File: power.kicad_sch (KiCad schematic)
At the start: 28 parts, among them J3 Conn_01x02_MountingPin, J4 Conn_01x02_Socket, J5 Conn_01x02_Socket, U3 TPS55287, U4 MPM3620A

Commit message: Power board complete v1.0
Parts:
- added C_in1, C_in3, C_in4: 10u, Capacitor_SMD:C_1206_3216Metric, symbol Device:C
- added J5, J6: 5V, Connector_JST:JST_XH_S2B-XH-A_1x02_P2.50mm_Horizontal, symbol Connector:Conn_01x02_Socket
- added J8, J9: 12V, Connector_JST:JST_XH_S2B-XH-A_1x02_P2.50mm_Horizontal, symbol Connector:Conn_01x02_Socket
- added SW1: Pull Tag, LEOS:D2F-FL-A1, symbol Switch:SW_SPDT
- added SW2: Power Switch, Button_Switch_THT:SW_Slide_SPDT_Angled_CK_OS102011MA1Q, symbol Switch:SW_SPDT
- added TP5: 12V Test, TestPoint:TestPoint_Loop_D2.60mm_Drill0.9mm_Beaded, symbol Connector:TestPoint
- added TP6: GND Test Point, TestPoint:TestPoint_Loop_D2.60mm_Drill0.9mm_Beaded, symbol Connector:TestPoint
- C_COMP1: value 36.5n -> 33n; footprint Capacitor_SMD:C_0805_2012Metric -> Capacitor_SMD:C_0603_1608Metric; Digikey (none) -> 1276-2040-1-ND; MPN (none) -> CL10B333KB8NFNC; Manufacturer (none) -> Samsung Electro-Mechanics
- C_COMP2: value 18.2n -> 15n; footprint Capacitor_SMD:C_0805_2012Metric -> Capacitor_SMD:C_0603_1608Metric; Digikey (none) -> 1276-1277-1-ND; MPN (none) -> CL10B153KB8NNNC; Manufacturer (none) -> Samsung Electro-Mechanics
- C_SYNC1: footprint Capacitor_SMD:C_0805_2012Metric -> Capacitor_SMD:C_0603_1608Metric; Digikey (none) -> 1276-1063-1-ND; MPN (none) -> CL10B473KB8NNNC; Manufacturer (none) -> Samsung Electro-Mechanics
- C_VCC1: Digikey (none) -> 1276-2970-1-ND; MPN (none) -> CL21B475KOFNFNE; Manufacturer (none) -> Samsung Electro-Mechanics
- C_in2: value 47u -> 10u; footprint Capacitor_SMD:C_0805_2012Metric -> Capacitor_SMD:C_1206_3216Metric; Digikey (none) -> 1276-6767-1-ND; MPN (none) -> CL31B106KBHNNNE; Manufacturer (none) -> Samsung Electro-Mechanics
- J3: value Conn_01x02_MountingPin -> Power Input; footprint Connector_AMASS:AMASS_XT60IPW-M_1x03_P7.20mm_Horizontal -> LEOS:AMASS_XT60IPW-M_1x03_P7.20mm_Horizontal; symbol Connector_Generic_MountingPin:Conn_01x02_MountingPin -> Connector:Conn_01x02_Socket
- J4: renamed from J5; value Conn_01x02_Socket -> 5V; Digikey (none) -> 455-S2B-XH-A-ND; MPN (none) -> S2B-XH-A; Manufacturer (none) -> JST
- J7: renamed from J4; value Conn_01x02_Socket -> 12V; Digikey (none) -> 455-S2B-XH-A-ND; MPN (none) -> S2B-XH-A; Manufacturer (none) -> JST
- L1: Digikey (none) -> 587-2960-1-ND; MPN (none) -> NRS8030T100MJGJ; Manufacturer (none) -> Taiyo Yuden
- NT1: footprint (none) -> NetTie:NetTie-2_SMD_Pad0.5mm
- R5, R6, RUP1: Digikey (none) -> 541-100KCCT-ND; MPN (none) -> CRCW0805100KFKEA; Manufacturer (none) -> Vishay Dale
- R7: Digikey (none) -> 541-19.1KCCT-ND; MPN (none) -> CRCW080519K1FKEA; Manufacturer (none) -> Vishay Dale
- RBT1: value 11.1k -> 11k; Digikey (none) -> 541-CRCW080511K0FKEACCT-ND; MPN (none) -> CRCW080511K0FKEAC; Manufacturer (none) -> Vishay Dale
- RP1: value 10k -> 11k; symbol Device:R_US -> Device:R; Digikey (none) -> 541-CRCW080511K0FKEACCT-ND; MPN (none) -> CRCW080511K0FKEAC; Manufacturer (none) -> Vishay Dale
- R_CDC1: Digikey (none) -> 541-20.0KCCT-ND; MPN (none) -> CRCW080520K0FKEA; Manufacturer (none) -> Vishay Dale
- R_COMP1: value 7.23k -> 7.5k; Digikey (none) -> 541-CRCW08057K50FKEACCT-ND; MPN (none) -> CRCW08057K50FKEAC; Manufacturer (none) -> Vishay Dale
- R_FSW1: value 9.3k -> 9.1k; Digikey (none) -> 541-9.10KCCT-ND; MPN (none) -> CRCW08059K10FKEA; Manufacturer (none) -> Vishay Dale
- R_SNS1: Digikey (none) -> 541-WSLP0805R0160FEACT-ND; MPN (none) -> WSLP0805R0160FEA; Manufacturer (none) -> Vishay Dale
- renumbered Cout1 to C_out1
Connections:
- net +12V: now also J8.1 (Pin_1), J9.1 (Pin_1), TP5.1
- net +5V: now also J5.1 (Pin_1), J6.1 (Pin_1)
- net GND: now also C_VCC1.2, C_in1.2, C_in3.2, C_in4.2, J5.2 (Pin_2), J6.2 (Pin_2), J8.2 (Pin_2), J9.2 (Pin_2), SW1.2 (B), SW2.3 (C), TP6.1
- net GNDA: no longer C_VCC1.2
- net VDC: now also C_in1.1, C_in3.1, C_in4.1; no longer RP1.1
- net at C_VCC1.1, U3.18 (VCC): now also RP1.1
- net at RP1.2: now also SW2.1 (A); no longer U3.1 (EN/UVLO)
- new net: SW1.3 (C), SW2.2 (B)
- new net EN: SW1.1 (A), U3.1 (EN/UVLO)
- no-connect marks 4 -> 3
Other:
- note added: "Power Connectors"
- note added: "Vin: 11-24V (3S to 6S LiPo)"
- moved on the sheet: C_BOOT1, C_BOOT2, C_COMP1, C_COMP2, C_SYNC1, C_VCC1, C_in2, C_out1, C_out2, C_out3, Cin1, J4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

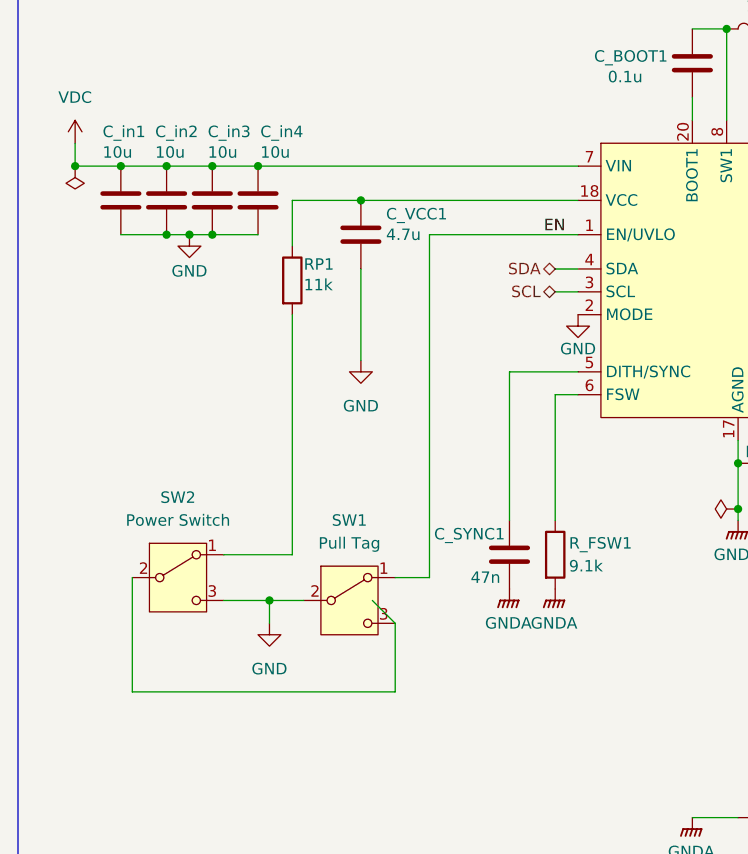
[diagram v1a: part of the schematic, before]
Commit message: v1.1 Fix UVLO and EN power source
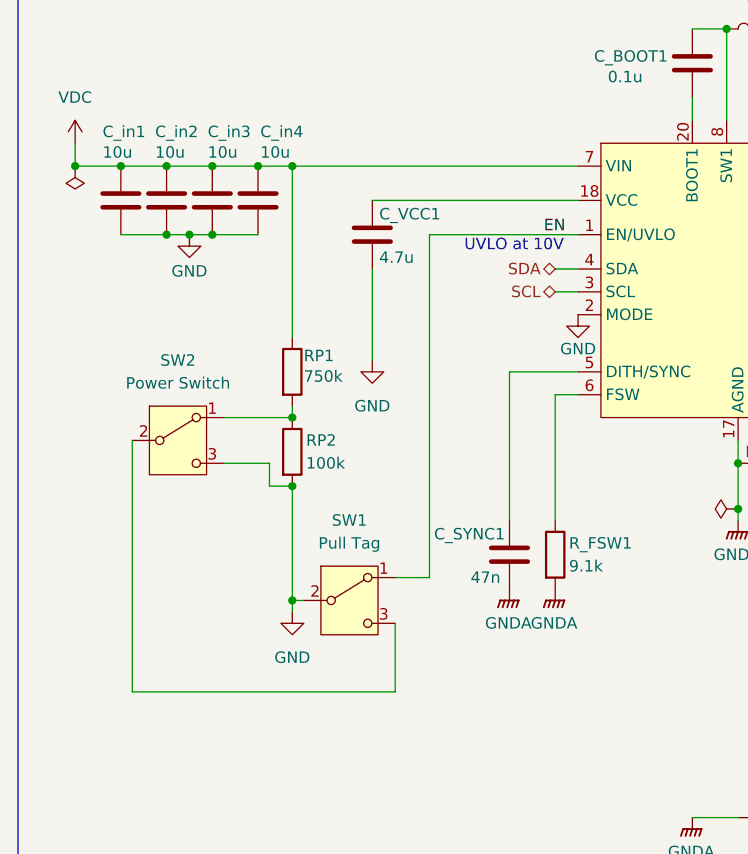
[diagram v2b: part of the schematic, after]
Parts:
- added RP2: 100k, Resistor_SMD:R_0805_2012Metric, symbol Device:R
- RP1: value 11k -> 750k; footprint Resistor_SMD:R_0805_2012Metric_Pad1.20x1.40mm_HandSolder -> Resistor_SMD:R_0805_2012Metric; Digikey 541-CRCW080511K0FKEACCT-ND -> 541-750KCCT-ND; MPN CRCW080511K0FKEAC -> CRCW0805750KFKEA
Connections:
- net GND: now also RP2.2
- net VDC: now also RP1.1
- net at C_VCC1.1, U3.18 (VCC): no longer RP1.1
- net at RP1.2, SW2.1 (A): now also RP2.1
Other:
- note added: "UVLO at 10V"
- moved on the sheet: C_VCC1, RP1, SW2
